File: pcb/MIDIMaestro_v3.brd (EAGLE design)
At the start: 61 x 88.3 mm, 38 parts, among them IC1 74LS133N, IC3 74LS138N, IC4 68B50, IC5 74LS04N, IC6 74*161, X1 MIDI_IN, X2 MIDI_THRU, X3 MIDI_OUT, X4 EXPANSION_PORT_COCO

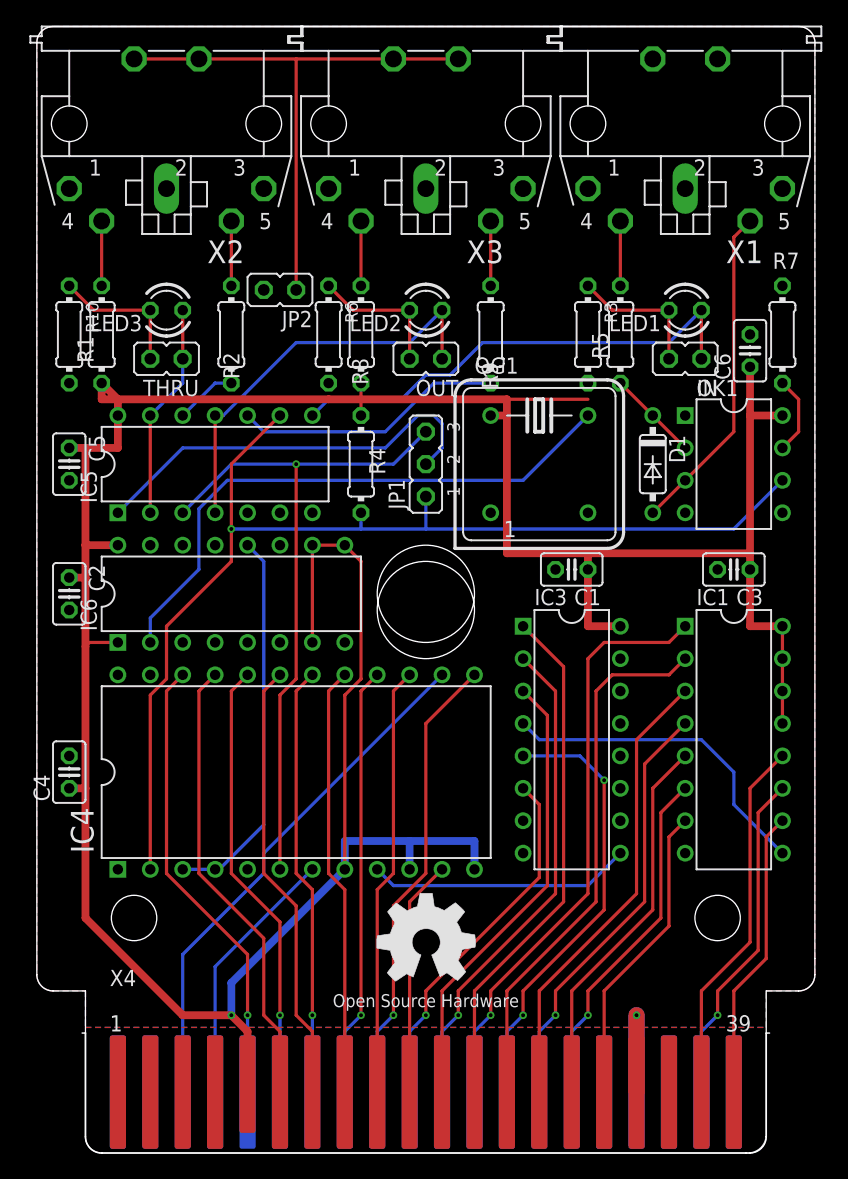
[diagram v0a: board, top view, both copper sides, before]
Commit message: Changed name, Added Dragon variant
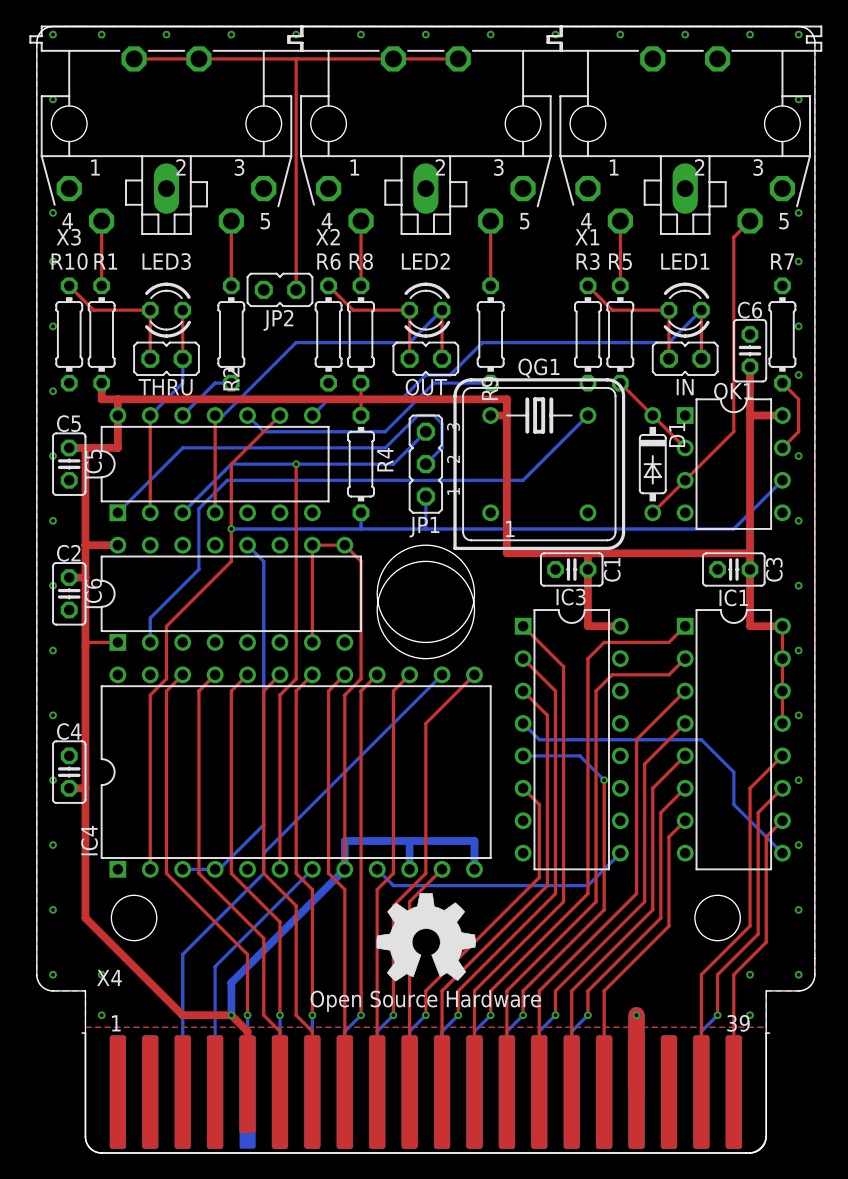
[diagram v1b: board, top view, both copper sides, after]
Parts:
- D1: value 1N4148DO35-7 -> 1N4148
- IC6: value 74*161 -> 74LS161
- R1, R2, R5, R8, R9: value 220R -> 220
- R4: value 270R -> 270
- X2: value MIDI_THRU -> MIDI_OUT
- X3: value MIDI_OUT -> MIDI_THRU
- moved X2 20.3 mm to (0.00, 80.6)
- moved X3 20.3 mm to (-20.3, 80.6)
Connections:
- net N$1: now also X2.5; no longer X3.5
- net N$10: now also X3.5; no longer X2.5
- net N$13: now also X3.4; no longer X2.4
- net N$3: now also X2.4; no longer X3.4
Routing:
- net VCC: track 258.6 -> 250.5 mm
- net GND: vias 1 -> 46
